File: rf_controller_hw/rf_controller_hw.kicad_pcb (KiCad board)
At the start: 2 copper layers, 114.3 x 69.8 mm, 5 parts, among them J1 NRF24L01, SW10 JOYSTICK_BUTTON, SW8 SW_DIP_x05

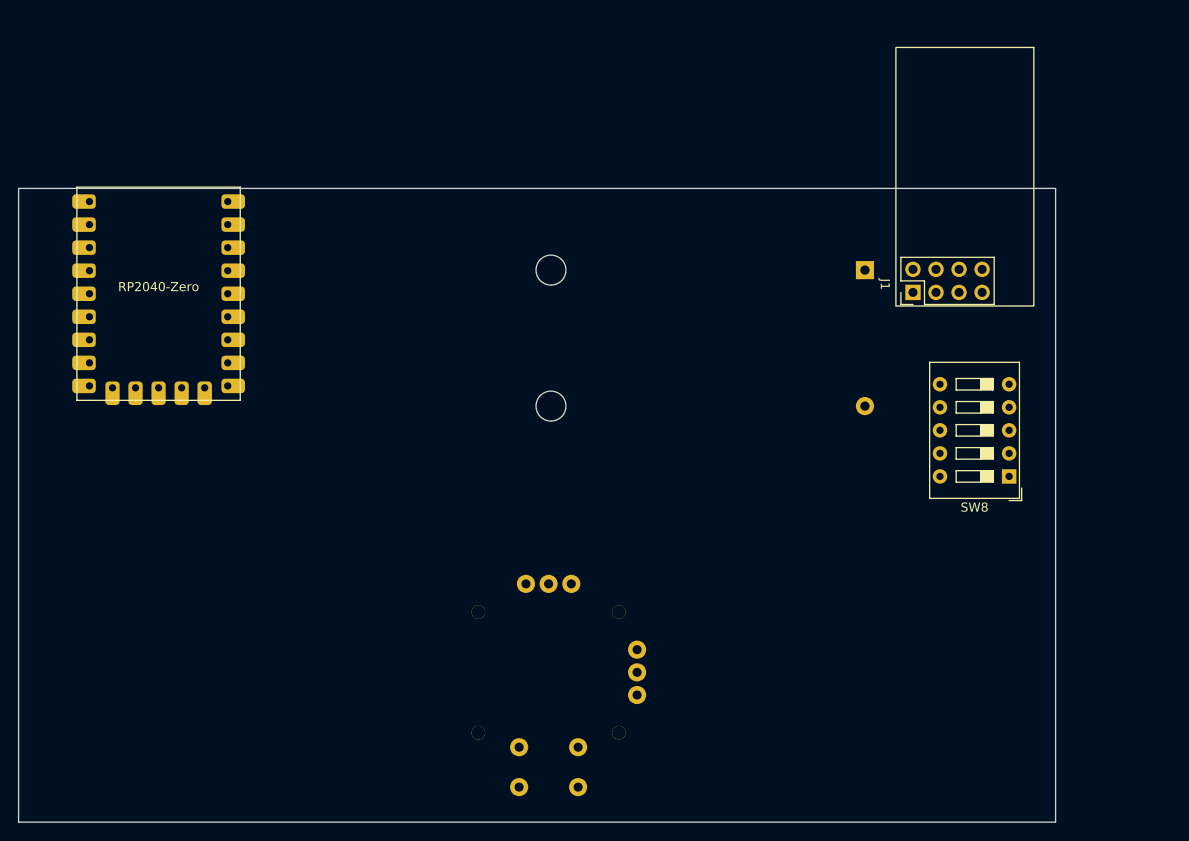
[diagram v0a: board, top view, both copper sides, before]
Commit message: Changed to mechanical keyboard switches
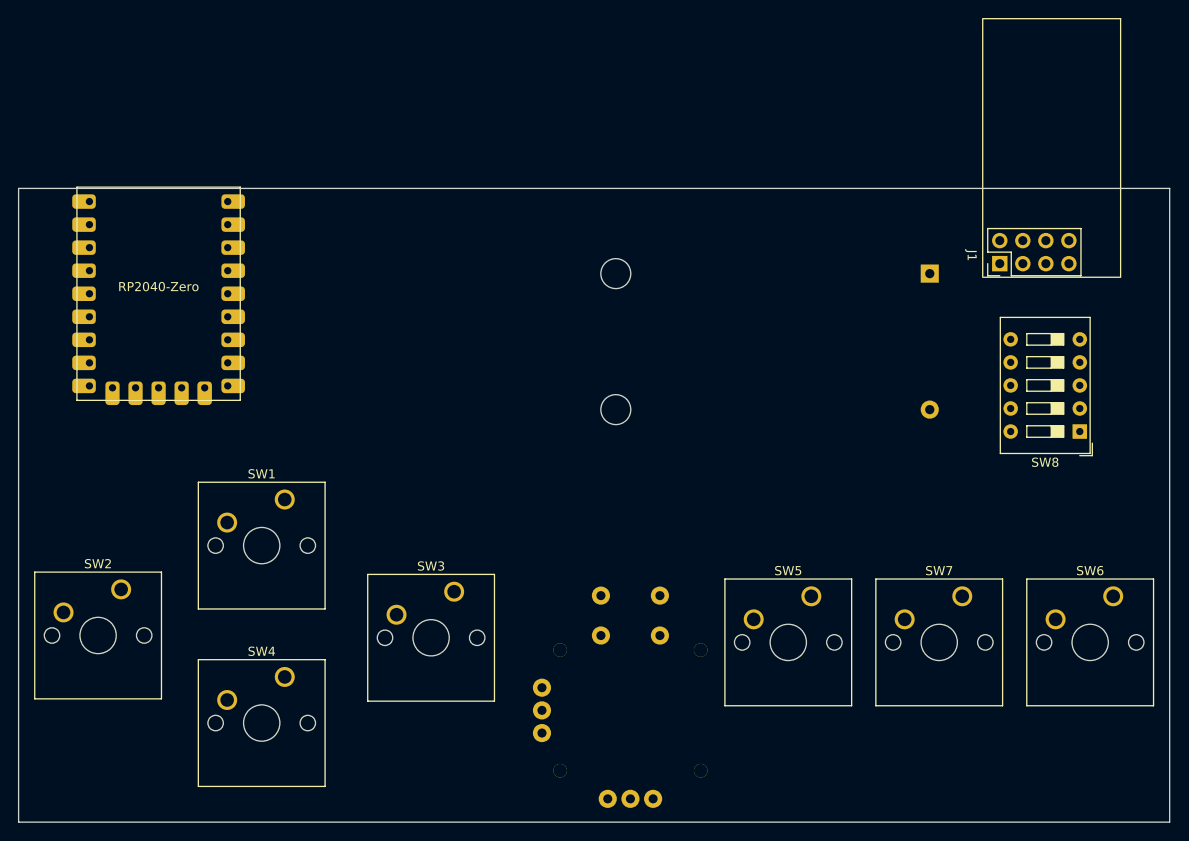
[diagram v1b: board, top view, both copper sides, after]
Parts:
- added SW1: SW_Push, Button_Switch_Keyboard:SW_Cherry_MX_1.00u_PCB, F.Cu at (118.2, 80.0)
- added SW2: SW_Push, Button_Switch_Keyboard:SW_Cherry_MX_1.00u_PCB, F.Cu at (100.2, 89.9)
- added SW3: SW_Push, Button_Switch_Keyboard:SW_Cherry_MX_1.00u_PCB, F.Cu at (136.9, 90.2)
- added SW4: SW_Push, Button_Switch_Keyboard:SW_Cherry_MX_1.00u_PCB, F.Cu at (118.2, 99.6)
- added SW5: SW_Push, Button_Switch_Keyboard:SW_Cherry_MX_1.00u_PCB, F.Cu at (176.3, 90.7)
- added SW6: SW_Push, Button_Switch_Keyboard:SW_Cherry_MX_1.00u_PCB, F.Cu at (209.6, 90.7)
- added SW7: SW_Push, Button_Switch_Keyboard:SW_Cherry_MX_1.00u_PCB, F.Cu at (192.9, 90.7)
- moved J1 10.1 mm to (210.4, 27.0)
- moved SW10 9.94 mm to (156.3, 103.3), turned to 180 degrees
- moved SW8 9.23 mm to (205.9, 72.5)
- moved BT1 7.16 mm to (184.5, 79.1)
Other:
- board size 114.3 x 69.8 mm -> 126.9 x 69.8 mm

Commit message: Finished first draft:
 - Spread out buttons on right
 - Added power switch
 - Added a budget logo
 - Added gerbers for PCB order
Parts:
- added G***: LOGO, rf_controller_hw:rf_commander, F.Cu at (171.2, 64.8)
- added SW10: SW_SPDT, Connector_PinHeader_2.54mm:PinHeader_1x03_P2.54mm_Vertical, F.Cu at (213.1, 73.4)
- SW1: renamed from SW2; footprint Button_Switch_Keyboard:SW_Cherry_MX_1.00u_PCB -> Button_Switch_THT:SW_PUSH_6mm_H5mm
- SW2: renamed from SW1; footprint Button_Switch_Keyboard:SW_Cherry_MX_1.00u_PCB -> Button_Switch_THT:SW_PUSH_6mm_H5mm
- SW3: renamed from SW4; footprint Button_Switch_Keyboard:SW_Cherry_MX_1.00u_PCB -> Button_Switch_THT:SW_PUSH_6mm_H5mm
- SW4: renamed from SW3; footprint Button_Switch_Keyboard:SW_Cherry_MX_1.00u_PCB -> Button_Switch_THT:SW_PUSH_6mm_H5mm
- SW5: renamed from SW8; moved to B.Cu
- SW6: renamed from SW5; footprint Button_Switch_Keyboard:SW_Cherry_MX_1.00u_PCB -> Button_Switch_THT:SW_PUSH_6mm_H5mm
- SW8: renamed from SW6; footprint Button_Switch_Keyboard:SW_Cherry_MX_1.00u_PCB -> Button_Switch_THT:SW_PUSH_6mm_H5mm
- SW9: renamed from SW7; footprint Button_Switch_Keyboard:SW_Cherry_MX_1.00u_PCB -> Button_Switch_THT:SW_PUSH_6mm_H5mm
- moved SW5 105.0 mm to (100.8, 73.9)
- moved SW8 21.2 mm to (188.5, 93.0)
- moved J1 19.9 mm to (210.2, 46.9)
- moved SW4 14.2 mm to (123.8, 95.5)
- moved SW9 11.6 mm to (202.5, 84.1)
- moved SW6 11.6 mm to (173.3, 101.9)
- moved SW3 8.52 mm to (112.3, 105.7)
- moved SW2 7.20 mm to (112.3, 84.1)
- moved SW1 5.67 mm to (100.9, 95.5)
- moved SW7 5.21 mm to (153.8, 98.7)
- renumbered SW10 to SW7
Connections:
- BT1 pad 1: +3V0 -> /BATT_NOSW
- RZ1 pad 13: /DIP5 -> /DIP1
- RZ1 pad 14: /DIP4 -> /DIP2
- RZ1 pad 16: /DIP2 -> /DIP4
- RZ1 pad 17: /DIP1 -> /DIP5
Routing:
- net +3V0: track 0.00 -> 206.0 mm, vias 0 -> 3
- net /SW7: track 0.00 -> 165.0 mm
- net /SW6: track 0.00 -> 145.5 mm
- net /SW5: track 0.00 -> 124.5 mm
- net /JOY_Y: track 0.00 -> 121.8 mm, vias 0 -> 2
- net /SPI_MOSI: track 0.00 -> 109.2 mm
- net /SPI_NCS: track 0.00 -> 108.8 mm
- net /SPI_MISO: track 0.00 -> 106.5 mm
- net /SPI_SCK: track 0.00 -> 106.0 mm
- net /NRF_CE: track 0.00 -> 103.8 mm
- net /JOY_X: track 0.00 -> 96.4 mm, vias 0 -> 2
- net /JOY_PB: track 0.00 -> 96.4 mm, vias 0 -> 2
- net /SW3: track 0.00 -> 77.8 mm
- net /SW4: track 0.00 -> 68.6 mm
- net /SW2: track 0.00 -> 62.4 mm
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- added copper zone on B.Cu, net GND
- added copper zone on F.Cu, net GND
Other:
- board size 126.9 x 69.8 mm -> 127 x 69.8 mm
- board text added: "ON"

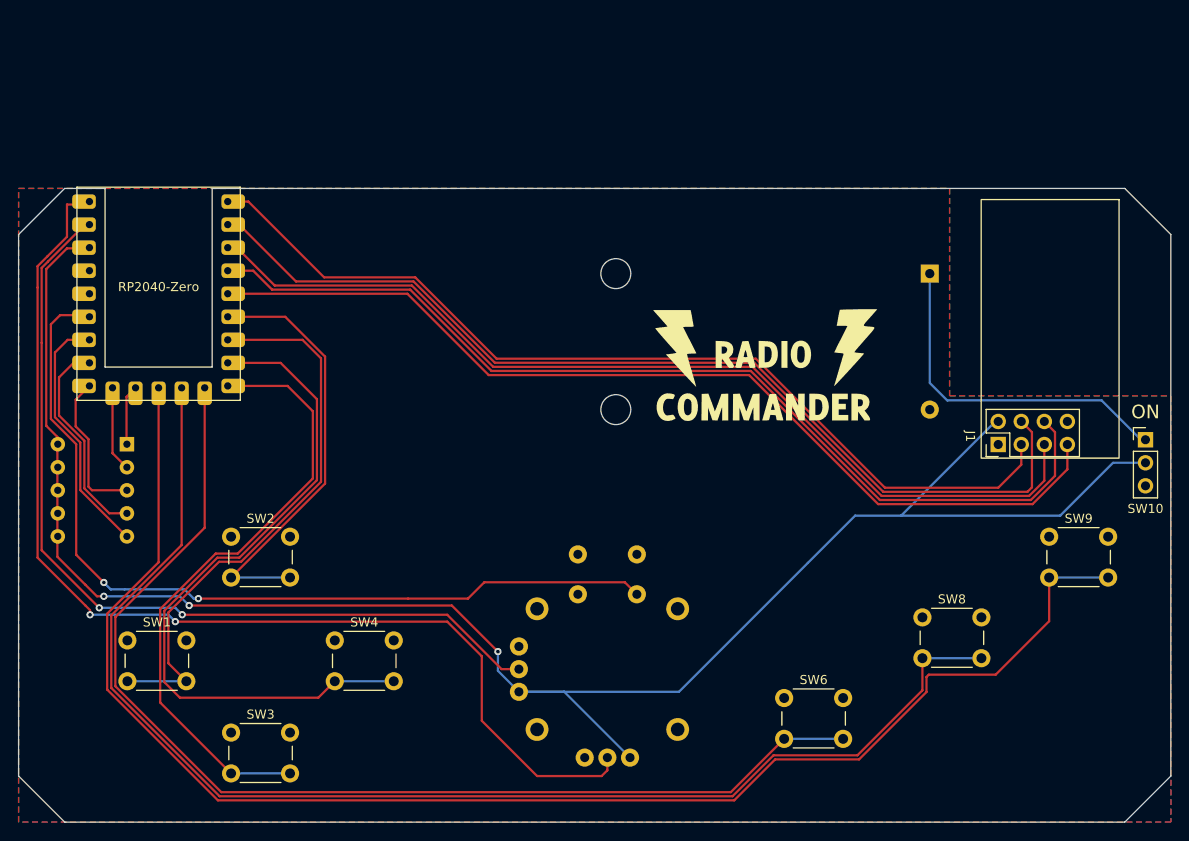
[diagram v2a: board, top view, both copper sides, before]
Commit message: Fixed a bug in the first board:
Fixed bug in RP2040-Zero pinout
Added better logo
Re-added mounting holes
Switched to smaller joystick
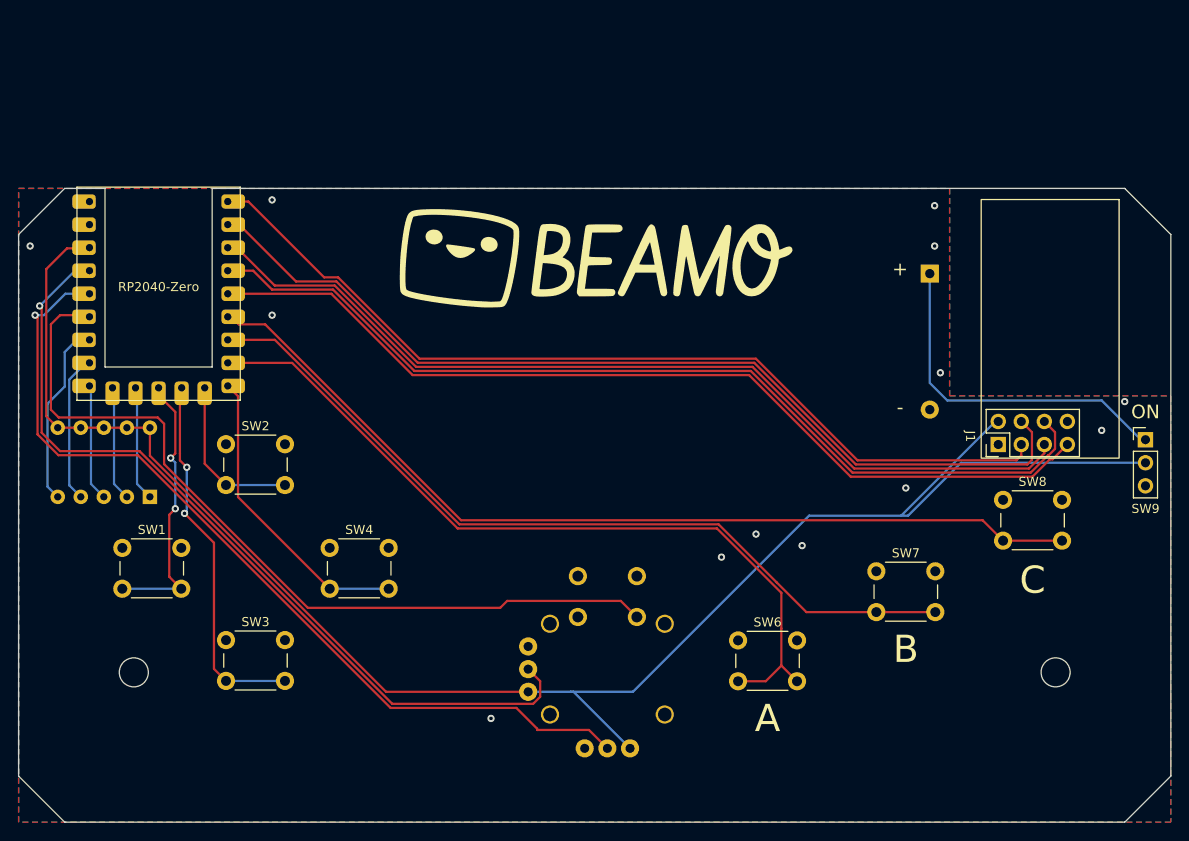
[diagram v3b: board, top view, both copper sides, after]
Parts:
- removed the G*** at (171.2, 64.8)
- added G***: LOGO, rf_controller_hw:beamo, F.Cu at (152.4, 53.3)
- added REF**: MountingHole_3.2mm_M3, MountingHole:MountingHole_3.2mm_M3, F.Cu at (203.2, 99.1)
- added REF**: MountingHole_3.2mm_M3, MountingHole:MountingHole_3.2mm_M3, F.Cu at (101.6, 99.1)
- RZ1: footprint rp2040-zero:RP2040-Zero -> rf_controller_hw:RP2040-Zero
- SW5: renamed from SW7; footprint rf_controller_hw:Joystick_Button -> rf_controller_hw:ALPS_RKJXV1224
- moved SW1 10.2 mm to (100.3, 85.3)
- moved SW4 10.2 mm to (123.2, 85.3)
- moved SW2 10.2 mm to (111.8, 73.9)
- moved SW3 10.2 mm to (111.8, 95.5)
- moved SW6 8.13 mm to (168.2, 95.5)
- moved SW7 7.18 mm to (183.4, 87.9)
- moved SW8 6.51 mm to (197.4, 80.0)
- moved SW10 6.33 mm to (103.4, 79.7), turned to 90 degrees
- renumbered SW5 to SW10, SW8 to SW7, SW9 to SW8, SW10 to SW9
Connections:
- RZ1 pad 10: /SW5 -> /SW2
- RZ1 pad 11: /SW6 -> /SW3
- RZ1 pad 12: /SW7 -> /SW1
- RZ1 pad 22: unconnected-(RZ1-Pad22) -> GND
- RZ1 pad 23: GND -> unconnected-(RZ1-Pad23)
- RZ1 pad 6: /SW1 -> /SW8
- RZ1 pad 7: /SW2 -> /SW7
- RZ1 pad 8: /SW3 -> /SW6
- SW1 pad 2: /SW2 -> /SW1
- SW2 pad 2: /SW1 -> /SW2
- SW3 pad 2: /SW4 -> /SW3
- SW4 pad 2: /SW3 -> /SW4
- SW6 pad 2: /SW5 -> /SW6
- SW7 pad 2: /SW6 -> /SW7
- SW8 pad 2: /SW7 -> /SW8
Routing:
- net /SW5: track 124.5 -> 0.00 mm
- net /SW8: track 0.00 -> 102.2 mm
- net /SW7: track 165.0 -> 90.4 mm
- net /SW6: track 145.5 -> 87.5 mm
- net /SW2: track 62.4 -> 18.2 mm
- net /SW3: track 77.8 -> 41.2 mm, vias 0 -> 2
- net /SW4: track 68.6 -> 33.5 mm
- net /JOY_Y: track 121.8 -> 97.5 mm, vias 2 -> 1
- net /SW1: track 47.7 -> 30.7 mm, vias 0 -> 2
- net +3V0: track 206.0 -> 192.1 mm, vias 3 -> 0
- net /DIP5: track 27.9 -> 20.5 mm
- net /DIP4: track 23.2 -> 16.4 mm
- net /DIP1: track 6.62 -> 12.7 mm
- net /JOY_PB: track 96.4 -> 91.4 mm, vias 2 -> 0
- net /SPI_NCS: track 108.8 -> 104.5 mm
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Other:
- board text added: "A"
- board text added: "B"
- board text added: "C"
